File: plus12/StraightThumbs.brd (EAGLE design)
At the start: 118.7 x 54 mm, 14 parts

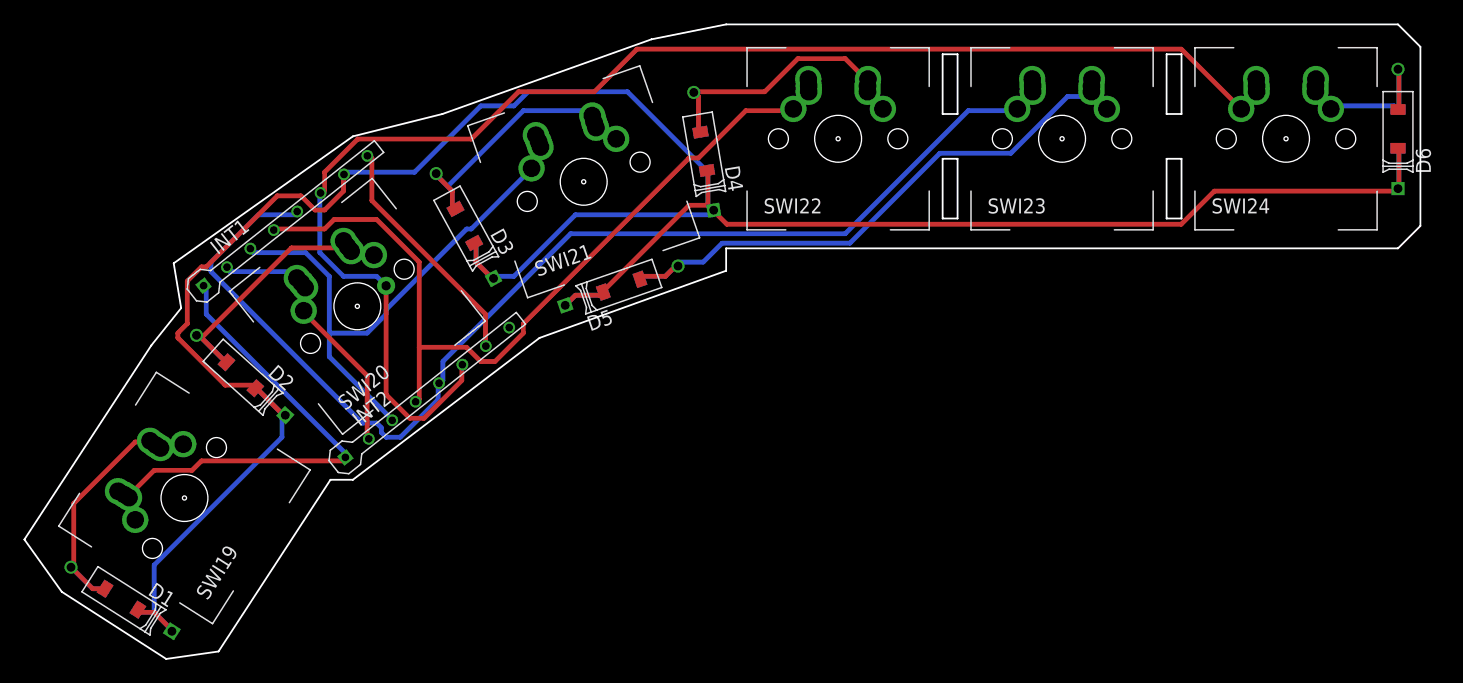
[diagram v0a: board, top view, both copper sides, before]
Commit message: Moving diode to inline position
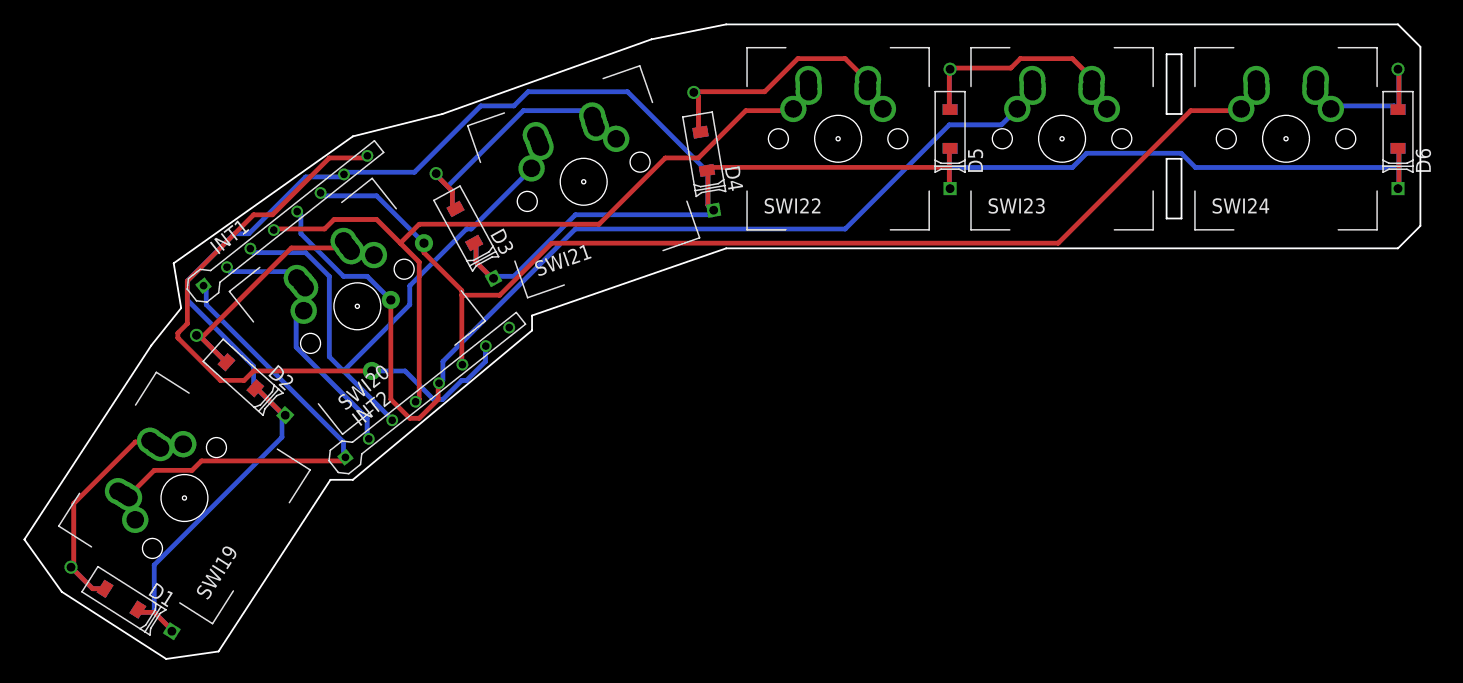
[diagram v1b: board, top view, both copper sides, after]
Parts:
- moved D5 31.0 mm to (79.4, 46.4), turned to 90 degrees
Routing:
- net N$14: track 20.4 -> 56.6 mm, vias 0 -> 1
- net N$5: track 49.1 -> 20.6 mm
- net N$12: track 121.3 -> 99.5 mm
- net N$13: track 227.9 -> 211.1 mm
- net N$11: track 102.4 -> 90.9 mm, vias 0 -> 1
- net N$10: track 72.4 -> 68.8 mm
- net N$7: track 44.9 -> 44.0 mm
- net N$9: track 49.7 -> 50.6 mm
- net N$8: track 24.1 -> 24.7 mm
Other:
- outline, holes or cut-outs redrawn

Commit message: Kobe beefing it up
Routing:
- net N$14: track 56.6 -> 20.4 mm, vias 1 -> 0
- net N$11: track 90.9 -> 112.7 mm, vias 1 -> 2
- net N$13: track 211.1 -> 192.3 mm
- net N$12: track 99.5 -> 105.8 mm, vias 1 -> 3
- net N$10: track 68.8 -> 74.5 mm
- net N$5: track 20.6 -> 21.5 mm
- net N$8: track 24.7 -> 25.5 mm
- net N$3: track 22.4 -> 23.0 mm
- net N$7: track 44.0 -> 44.5 mm

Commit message: Updates, BEFORE C5/6 Move
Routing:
- net N$11: track 112.7 -> 90.1 mm, vias 2 -> 0
- net N$9: track 50.8 -> 65.1 mm, vias 0 -> 1
- net N$13: track 192.3 -> 204.0 mm, vias 0 -> 2
- net N$12: track 105.8 -> 102.1 mm, vias 3 -> 0
- net N$10: track 74.5 -> 76.6 mm
- net N$3: track 23.0 -> 23.9 mm
- net N$7: track 44.5 -> 45.1 mm
